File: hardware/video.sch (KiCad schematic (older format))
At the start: 29 parts, among them U4 74HC4053, U5 74HC86, U6 74HC4053, U7 LM1881, U8 THS7375

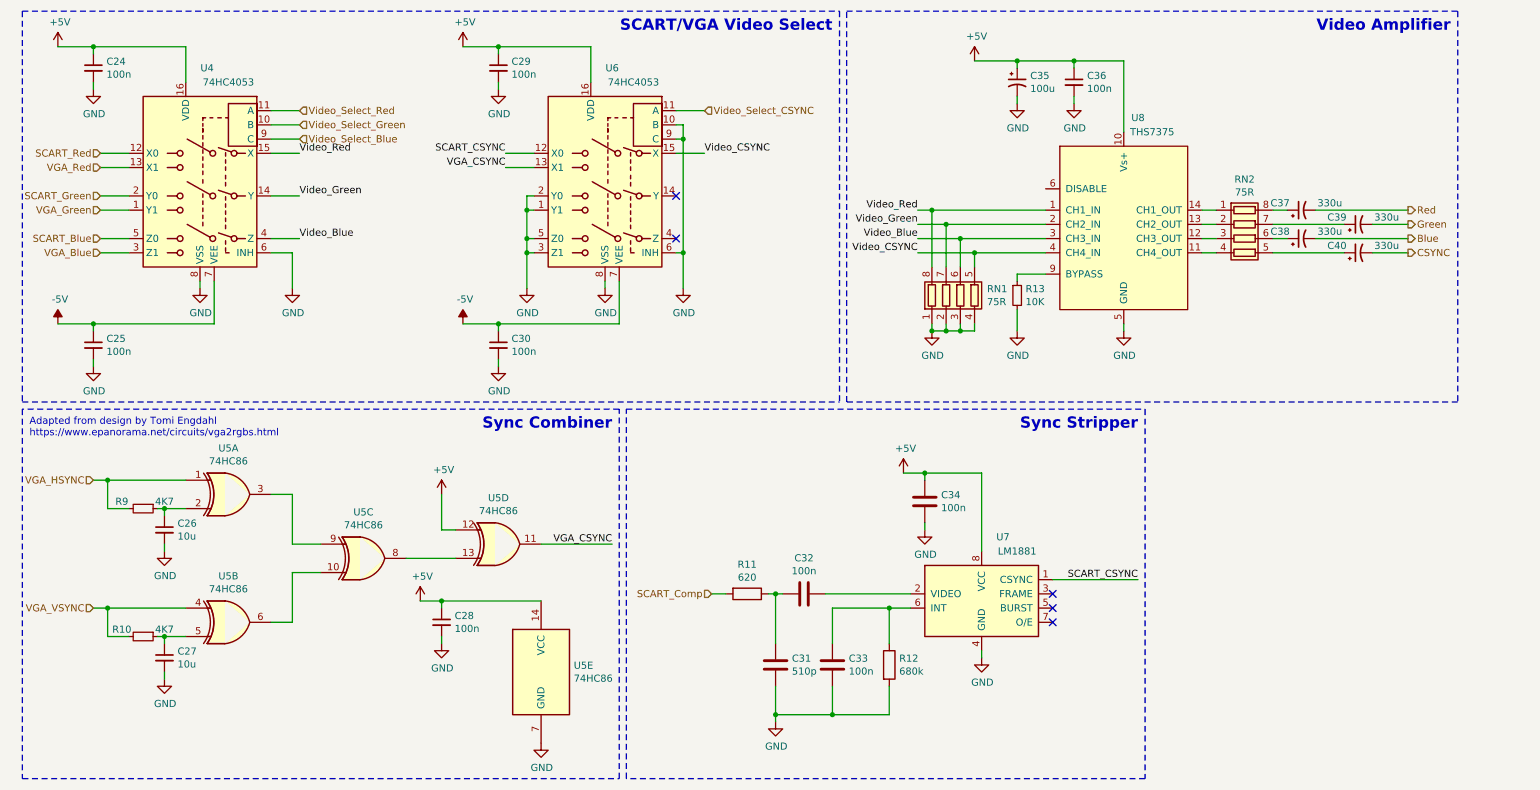
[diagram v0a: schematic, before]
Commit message: Schematic mainly done. Working on PCB layout in isolated blocks.
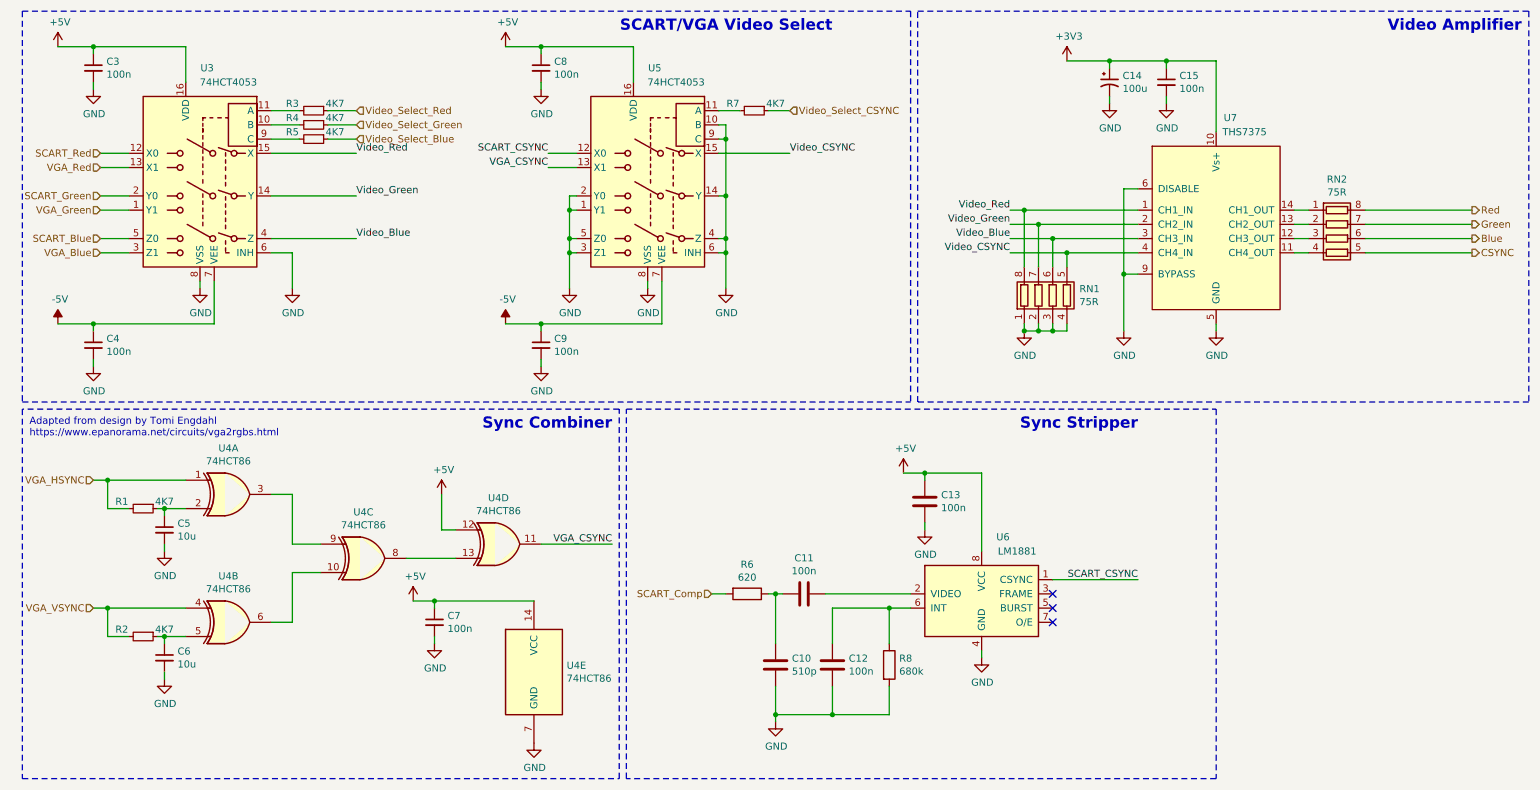
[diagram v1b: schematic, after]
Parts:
- removed C37, C38, C39, C40: 330u, Capacitor_SMD:CP_Elec_10x10.5, symbol Device:CP1_Small
- removed R13: 10K, Resistor_SMD:R_0603_1608Metric, symbol Device:R_Small
- removed U6: 74HC4053, Package_SO:TSSOP-14_4.4x5mm_P0.65mm, symbol Analog_Switch:CD4053B
- added R3, R4, R5, R7: 4K7, Resistor_SMD:R_0603_1608Metric, symbol Device:R_Small
- added U5: 74HCT4053, Package_SO:SSOP-16_5.3x6.2mm_P0.65mm, symbol Analog_Switch:CD4053B
- U3: renamed from U4; value 74HC4053 -> 74HCT4053; footprint Package_SO:TSSOP-14_4.4x5mm_P0.65mm -> Package_SO:SSOP-16_5.3x6.2mm_P0.65mm
- U4: renamed from U5; value 74HC86 -> 74HCT86
- renumbered C31 to C10, C32 to C11, C33 to C12, C34 to C13, C35 to C14, C36 to C15, C24 to C3, C25 to C4, C26 to C5, C27 to C6, C28 to C7, C29 to C8, C30 to C9, R9 to R1, R10 to R2, R11 to R6, R12 to R8, U7 to U6, U8 to U7
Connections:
- net +5V: now also U5.16 (VDD); no longer C14.1, C15.1, U7.10 (Vs+)
- net -5V: now also U5.7 (VEE)
- net Blue: now also RN2.6 (R3.2)
- net CSYNC: now also RN2.5 (R4.2)
- net GND: now also U7.6 (DISABLE), U7.9 (BYPASS), U5.1 (Y1), U5.10 (B), U5.14 (Y), U5.2 (Y0), U5.3 (Z1), U5.4 (Z), U5.5 (Z0), U5.6 (INH), U5.8 (VSS), U5.9 (C)
- net Green: now also RN2.7 (R2.2)
- net Red: now also RN2.8 (R1.2)
- net SCART_CSYNC: now also U5.12 (X0)
- net VGA_CSYNC: now also U5.13 (X1)
- net Video_CSYNC: now also U5.15 (X)
- net Video_Select_Blue: now also R5.1; no longer U3.9 (C)
- net Video_Select_CSYNC: now also R7.1
- net Video_Select_Green: now also R4.1; no longer U3.10 (B)
- net Video_Select_Red: now also R3.1; no longer U3.11 (A)
- new net: R4.2, U3.10 (B)
- new net: R3.2, U3.11 (A)
- new net: R5.2, U3.9 (C)
- new net: R7.2, U5.11 (A)
- new net +3V3: C14.1, C15.1, U7.10 (Vs+)
- no-connect marks 5 -> 3
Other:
- moved on the sheet: C14, C15, C7, C8, C9, RN1, RN2, U4E, U7

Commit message: Completing the functionality of PCB layout. Require silkscreen placement still, though.
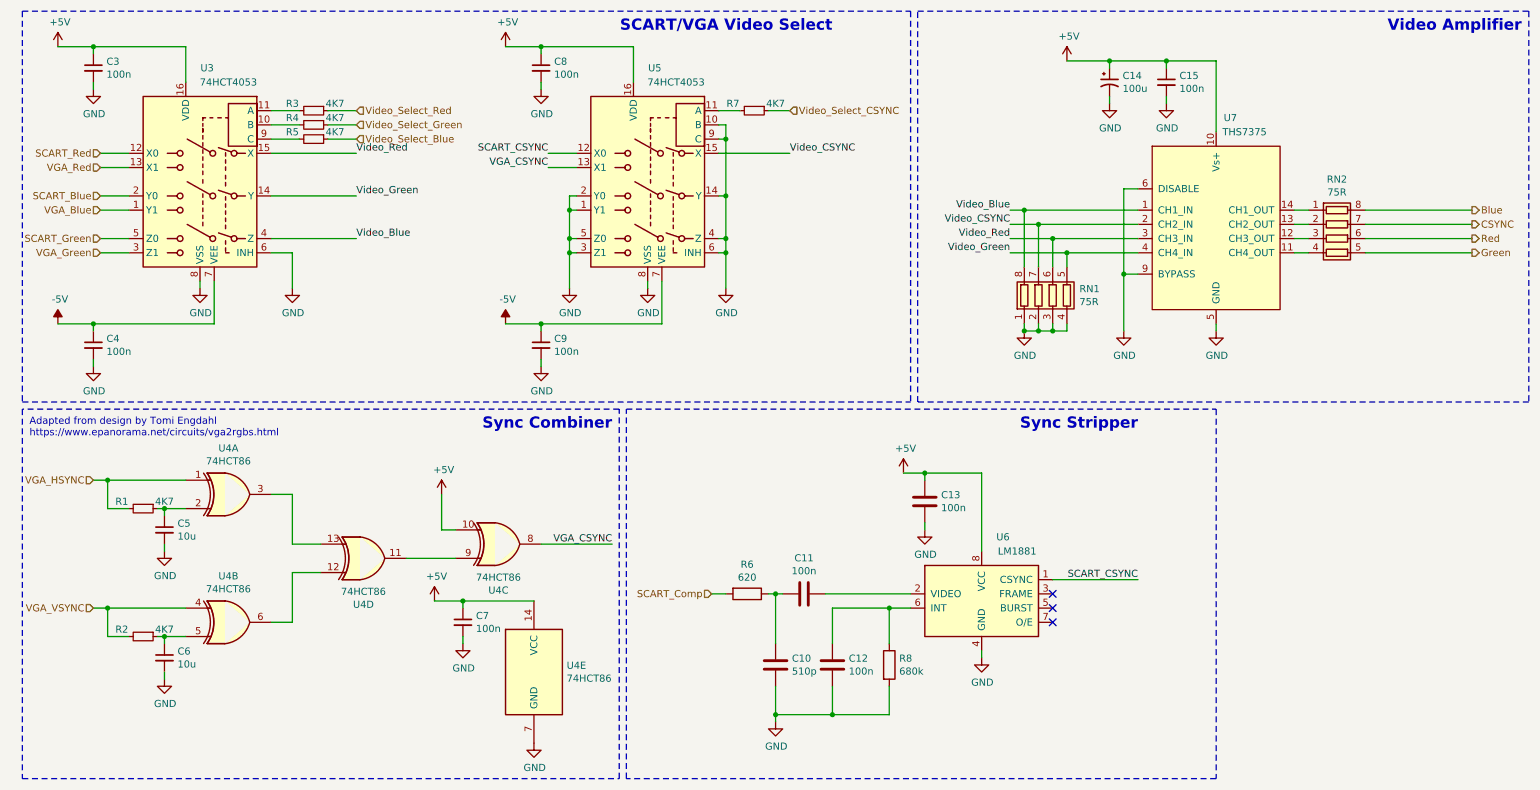
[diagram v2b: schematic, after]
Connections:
- net +3V3 is gone; now on net +5V: C14.1, C15.1, U7.10 (Vs+)
- net +5V: now also U4.10; no longer U4.12
- net Blue: now also RN2.8 (R1.2); no longer RN2.6 (R3.2)
- net CSYNC: now also RN2.7 (R2.2); no longer RN2.5 (R4.2)
- net Green: now also RN2.5 (R4.2); no longer RN2.7 (R2.2)
- net Red: now also RN2.6 (R3.2); no longer RN2.8 (R1.2)
- net SCART_Blue: now also U3.2 (Y0); no longer U3.5 (Z0)
- net SCART_Green: now also U3.5 (Z0); no longer U3.2 (Y0)
- net VGA_Blue: now also U3.1 (Y1); no longer U3.3 (Z1)
- net VGA_CSYNC: now also U4.8; no longer U4.11
- net VGA_Green: now also U3.3 (Z1); no longer U3.1 (Y1)
- net Video_Blue: now also RN1.8 (R1.2), U7.1 (CH1_IN); no longer RN1.6 (R3.2), U7.3 (CH3_IN)
- net Video_CSYNC: now also RN1.7 (R2.2), U7.2 (CH2_IN); no longer RN1.5 (R4.2), U7.4 (CH4_IN)
- net Video_Green: now also RN1.5 (R4.2), U7.4 (CH4_IN); no longer RN1.7 (R2.2), U7.2 (CH2_IN)
- net Video_Red: now also RN1.6 (R3.2), U7.3 (CH3_IN); no longer RN1.8 (R1.2), U7.1 (CH1_IN)
- net at U4.3: now also U4.13; no longer U4.9
- net at U4.6: now also U4.12; no longer U4.10
- new net: U4.11, U4.9
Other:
- moved on the sheet: C7, U4C, U4D
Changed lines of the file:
@@
 encoding utf-8
 Sheet 2 4
-Title "Video Section"
-Date "2020-04-03"
+Title "JAMMA2Console"
+Date "2020-04-06"
 Rev "1"
 Comp "Gold"
@@
 L power:+5V #PWR036
 U 1 1 5E7B890F
-P 3300 4700
-F 0 "#PWR036" H 3300 4550 50  0001 C CNN
-F 1 "+5V" H 3315 4873 50  0000 C CNN
-F 2 "" H 3300 4700 50  0001 C CNN
-F 3 "" H 3300 4700 50  0001 C CNN
-	1    3300 4700
+P 3450 4700
+F 0 "#PWR036" H 3450 4550 50  0001 C CNN
+F 1 "+5V" H 3465 4873 50  0000 C CNN
+F 2 "" H 3450 4700 50  0001 C CNN
+F 3 "" H 3450 4700 50  0001 C CNN
+	1    3450 4700
 	1    0    0    -1
 $EndComp
@@
 L Device:C_Small C?
 U 1 1 5E82D7A9
-P 3450 4850
+P 3650 4850
 AR Path="/5E46F7F7/5E82D7A9" Ref="C?"  Part="1"
 AR Path="/5E47086B/5E82D7A9" Ref="C7"  Part="1"
-F 0 "C7" H 3542 4896 50  0000 L CNN
-F 1 "100n" H 3542 4805 50  0000 L CNN
-F 2 "Capacitor_SMD:C_0603_1608Metric" H 3450 4850 50  0001 C CNN
-F 3 "~" H 3450 4850 50  0001 C CNN
-	1    3450 4850
-	1    0    0    -1
-$EndComp
-Wire Wire Line
-	3450 4750 3450 4700
-Wire Wire Line
-	3450 4700 4150 4700
-Connection ~ 3450 4700
-Wire Wire Line
-	3300 4700 3450 4700
-Wire Wire Line
-	3450 4950 3450 5000
+F 0 "C7" H 3742 4896 50  0000 L CNN
+F 1 "100n" H 3742 4805 50  0000 L CNN
+F 2 "Capacitor_SMD:C_0603_1608Metric" H 3650 4850 50  0001 C CNN
+F 3 "~" H 3650 4850 50  0001 C CNN
+	1    3650 4850
+	1    0    0    -1
+$EndComp
+Wire Wire Line
+	3650 4750 3650 4700
+Wire Wire Line
+	3650 4950 3650 5000
 $Comp
 L power:GND #PWR037
 U 1 1 5E83EB9D
-P 3450 5000
-F 0 "#PWR037" H 3450 4750 50  0001 C CNN
-F 1 "GND" H 3455 4827 50  0000 C CNN
-F 2 "" H 3450 5000 50  0001 C CNN
-F 3 "" H 3450 5000 50  0001 C CNN
-	1    3450 5000
-	1    0    0    -1
-$EndComp
+P 3650 5000
+F 0 "#PWR037" H 3650 4750 50  0001 C CNN
+F 1 "GND" H 3655 4827 50  0000 C CNN
+F 2 "" H 3650 5000 50  0001 C CNN
+F 3 "" H 3650 5000 50  0001 C CNN
+	1    3650 5000
+	1    0    0    -1
+$EndComp
+Text Label 7500 2050 2    50   ~ 0
+Video_CSYNC
+Wire Wire Line
+	7500 1950 7600 1950
+Wire Wire Line
+	8400 2050 7700 2050
+Wire Wire Line
+	8400 2150 7800 2150
+Text Label 7500 2150 2    50   ~ 0
+Video_Red
 Text Label 7500 2250 2    50   ~ 0
-Video_CSYNC
-Wire Wire Line
-	7500 1950 7600 1950
-Wire Wire Line
-	8400 2050 7700 2050
-Wire Wire Line
-	8400 2150 7800 2150
+Video_Green
 Text Label 7500 1950 2    50   ~ 0
-Video_Red
-Text Label 7500 2050 2    50   ~ 0
-Video_Green
-Text Label 7500 2150 2    50   ~ 0
 Video_Blue
 $Comp
@@
 $EndComp
 Text HLabel 10750 1950 2    50   Output ~ 0
-Red
-Text HLabel 10750 2050 2    50   Output ~ 0
-Green
-Text HLabel 10750 2150 2    50   Output ~ 0
 Blue
-Text HLabel 10750 2250 2    50   Output ~ 0
-CSYNC
 Wire Wire Line
 	9500 1950 9600 1950
@@
 Wire Wire Line
 	7800 2150 7800 2350
-$Comp
-L Device:R_Pack04 RN2
-U 1 1 5E8C2FCA
-P 9800 2150
-F 0 "RN2" V 9383 2150 50  0000 C CNN
-F 1 "75R" V 9474 2150 50  0000 C CNN
-F 2 "Resistor_SMD:R_Array_Convex_4x0603" V 10075 2150 50  0001 C CNN
-F 3 "~" H 9800 2150 50  0001 C CNN
-	1    9800 2150
-	0    1    1    0
-$EndComp
 Wire Wire Line
 	7500 2050 7700 2050
@@
 Text Label 4250 1550 2    50   ~ 0
 SCART_CSYNC
+Text HLabel 1100 1950 0    50   Input ~ 0
+VGA_Blue
 Text HLabel 1100 2250 0    50   Input ~ 0
-VGA_Blue
-Text HLabel 1100 1950 0    50   Input ~ 0
 VGA_Green
 Text HLabel 1100 1650 0    50   Input ~ 0
 VGA_Red
+Text HLabel 1100 2150 0    50   Input ~ 0
+SCART_Green
 Text HLabel 1100 1850 0    50   Input ~ 0
-SCART_Green
-Text HLabel 1100 2150 0    50   Input ~ 0
 SCART_Blue
 Text HLabel 1100 1550 0    50   Input ~ 0
@@
 L 74xx:74HC86 U4
 U 3 1 5E741D86
+P 3900 4300
+F 0 "U4" H 3900 4625 50  0000 C CNN
+F 1 "74HCT86" H 3900 4534 50  0000 C CNN
+F 2 "Package_SO:SOIC-14_3.9x8.7mm_P1.27mm" H 3900 4300 50  0001 C CNN
+F 3 "http://www.ti.com/lit/gpn/sn74HC86" H 3900 4300 50  0001 C CNN
+	3    3900 4300
+	1    0    0    1
+$EndComp
+$Comp
+L 74xx:74HC86 U4
+U 4 1 5E742930
 P 2950 4400
 F 0 "U4" H 2950 4725 50  0000 C CNN
@@
 F 2 "Package_SO:SOIC-14_3.9x8.7mm_P1.27mm" H 2950 4400 50  0001 C CNN
 F 3 "http://www.ti.com/lit/gpn/sn74HC86" H 2950 4400 50  0001 C CNN
-	3    2950 4400
-	1    0    0    -1
-$EndComp
-$Comp
-L 74xx:74HC86 U4
-U 4 1 5E742930
-P 3900 4300
-F 0 "U4" H 3900 4625 50  0000 C CNN
-F 1 "74HCT86" H 3900 4534 50  0000 C CNN
-F 2 "Package_SO:SOIC-14_3.9x8.7mm_P1.27mm" H 3900 4300 50  0001 C CNN
-F 3 "http://www.ti.com/lit/gpn/sn74HC86" H 3900 4300 50  0001 C CNN
-	4    3900 4300
-	1    0    0    -1
+	4    2950 4400
+	1    0    0    1
 $EndComp
 $Comp
@@
 	1    0    0    -1
 $EndComp
-$Comp
-L power:+3V3 #PWR052
-U 1 1 5E87CC9B
-P 7900 900
-F 0 "#PWR052" H 7900 750 50  0001 C CNN
-F 1 "+3V3" H 7915 1073 50  0000 C CNN
-F 2 "" H 7900 900 50  0001 C CNN
-F 3 "" H 7900 900 50  0001 C CNN
-	1    7900 900
-	1    0    0    -1
-$EndComp
 Wire Wire Line
 	8400 1800 8300 1800
@@
 Wire Wire Line
 	800  800  1050 800
+Connection ~ 3650 4700
+Wire Wire Line
+	3650 4700 4150 4700
+Wire Wire Line
+	3450 4700 3650 4700
+$Comp
+L Device:R_Pack04 RN2
+U 1 1 5E8C2FCA
+P 9800 2150
+F 0 "RN2" V 9383 2150 50  0000 C CNN
+F 1 "75R" V 9474 2150 50  0000 C CNN
+F 2 "Resistor_SMD:R_Array_Convex_4x0603" V 10075 2150 50  0001 C CNN
+F 3 "~" H 9800 2150 50  0001 C CNN
+	1    9800 2150
+	0    1    1    0
+$EndComp
+$Comp
+L power:+5V #PWR0158
+U 1 1 5ED32E3A
+P 7900 900
+F 0 "#PWR0158" H 7900 750 50  0001 C CNN
+F 1 "+5V" H 7915 1073 50  0000 C CNN
+F 2 "" H 7900 900 50  0001 C CNN
+F 3 "" H 7900 900 50  0001 C CNN
+	1    7900 900
+	1    0    0    -1
+$EndComp
+Text HLabel 10750 2050 2    50   Output ~ 0
+CSYNC
+Text HLabel 10750 2250 2    50   Output ~ 0
+Green
+Text HLabel 10750 2150 2    50   Output ~ 0
+Red
 $EndSCHEMATC

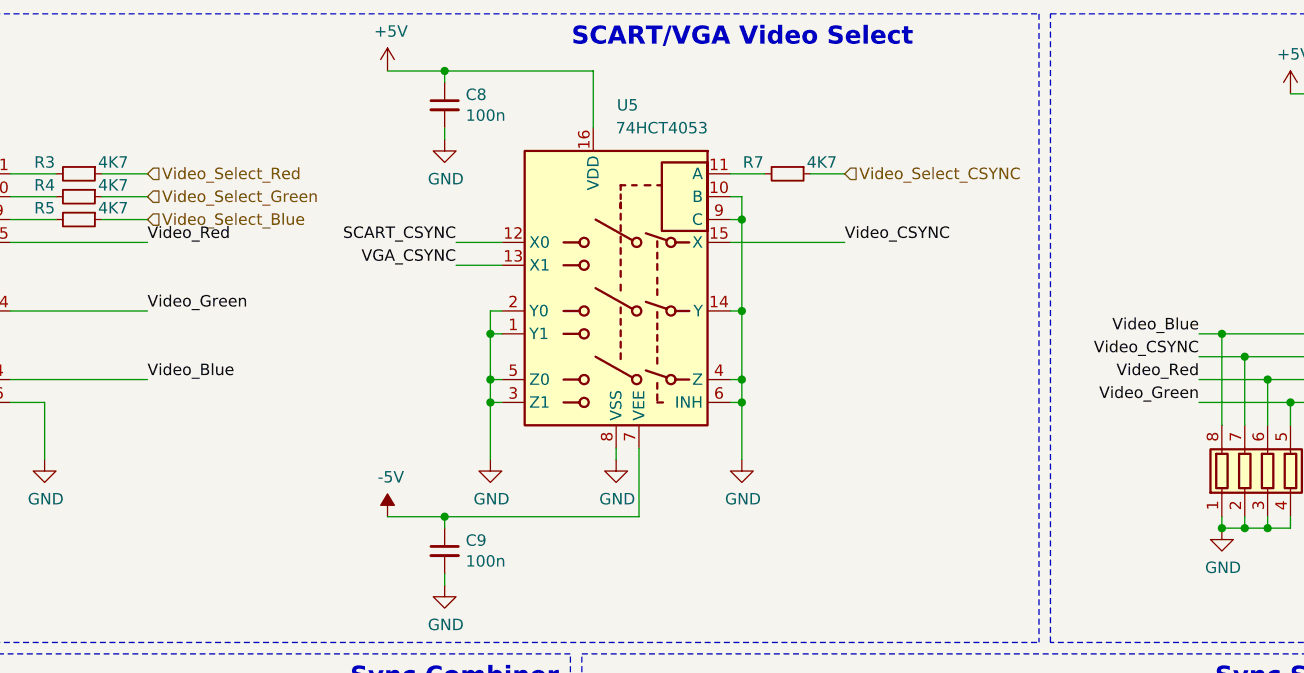
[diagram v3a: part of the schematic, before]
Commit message: Completing layout & minor edits for the main PCB. Added a project for the adapters to plug controllers into.
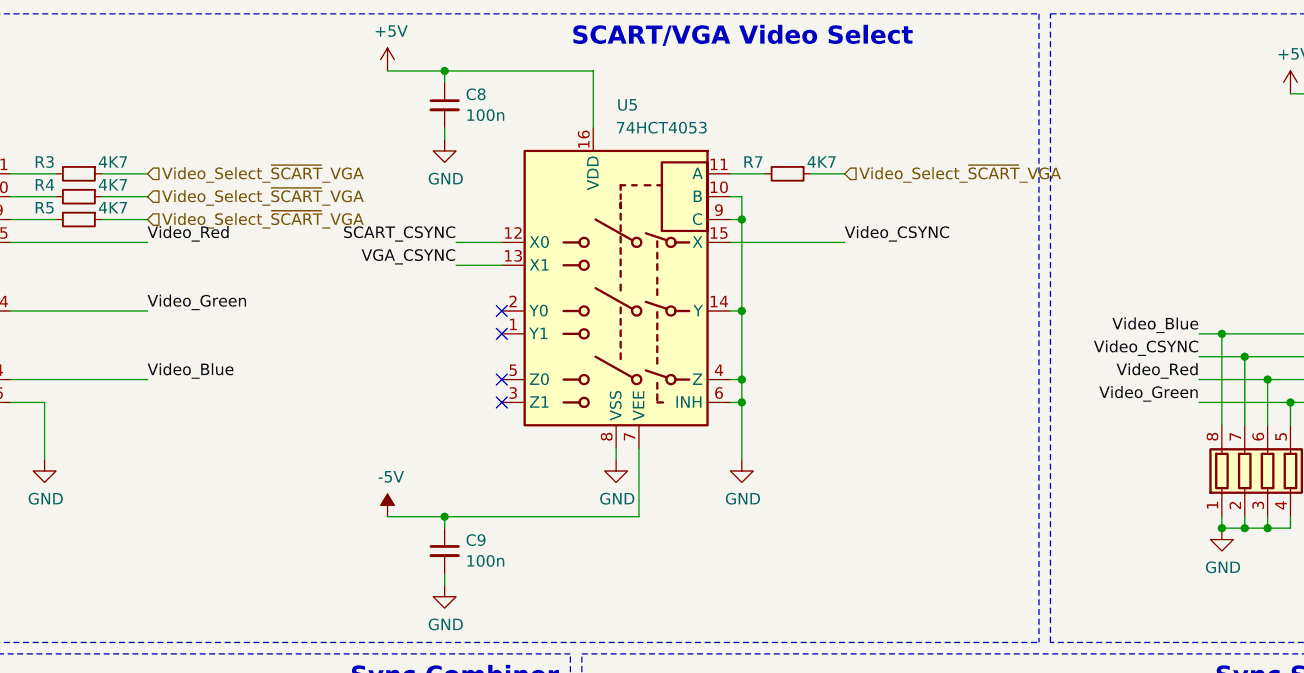
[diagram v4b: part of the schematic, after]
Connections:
- net Video_Select_CSYNC is gone; now on net Video_Select_~SCART~_VGA: R7.1
- net Video_Select_Green is gone; now on net Video_Select_~SCART~_VGA: R4.1
- net Video_Select_Red is gone; now on net Video_Select_~SCART~_VGA: R3.1
- net GND: no longer U5.1 (Y1), U5.2 (Y0), U5.3 (Z1), U5.5 (Z0)
- net Video_Select_Blue renamed Video_Select_~SCART~_VGA
- no-connect marks 3 -> 7
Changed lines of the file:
@@
 Wire Wire Line
 	5450 1550 5950 1550
-Text HLabel 5950 1250 2    50   Input ~ 0
-Video_Select_CSYNC
-Text HLabel 2900 1450 2    50   Input ~ 0
-Video_Select_Blue
-Text HLabel 2900 1350 2    50   Input ~ 0
-Video_Select_Green
-Text HLabel 2900 1250 2    50   Input ~ 0
-Video_Select_Red
 $Comp
 L power:GND #PWR046
@@
 Wire Wire Line
 	5450 2250 5500 2250
-$Comp
-L power:GND #PWR044
-U 1 1 5E661AE6
-P 4400 2500
-F 0 "#PWR044" H 4400 2250 50  0001 C CNN
-F 1 "GND" H 4405 2327 50  0000 C CNN
-F 2 "" H 4400 2500 50  0001 C CNN
-F 3 "" H 4400 2500 50  0001 C CNN
-	1    4400 2500
-	1    0    0    -1
-$EndComp
-Wire Wire Line
-	4400 2250 4400 2500
-Connection ~ 4400 2250
-Wire Wire Line
-	4400 2250 4450 2250
-Wire Wire Line
-	4400 2150 4400 2250
-Connection ~ 4400 2150
-Wire Wire Line
-	4400 2150 4450 2150
-Wire Wire Line
-	4400 1950 4400 2150
-Connection ~ 4400 1950
-Wire Wire Line
-	4400 1950 4450 1950
-Wire Wire Line
-	4400 1850 4400 1950
-Wire Wire Line
-	4450 1850 4400 1850
 Text Label 5950 1550 0    50   ~ 0
 Video_CSYNC
@@
 Text HLabel 10750 2150 2    50   Output ~ 0
 Red
+Text HLabel 2900 1250 2    50   Input ~ 0
+Video_Select_~SCART~_VGA
+Text HLabel 2900 1350 2    50   Input ~ 0
+Video_Select_~SCART~_VGA
+Text HLabel 2900 1450 2    50   Input ~ 0
+Video_Select_~SCART~_VGA
+Text HLabel 5950 1250 2    50   Input ~ 0
+Video_Select_~SCART~_VGA
+NoConn ~ 4450 1850
+NoConn ~ 4450 1950
+NoConn ~ 4450 2150
+NoConn ~ 4450 2250
 $EndSCHEMATC
